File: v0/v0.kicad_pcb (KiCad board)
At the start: 2 copper layers, 101.5 x 83 mm, 2 parts, among them CON1 SNES-CONN

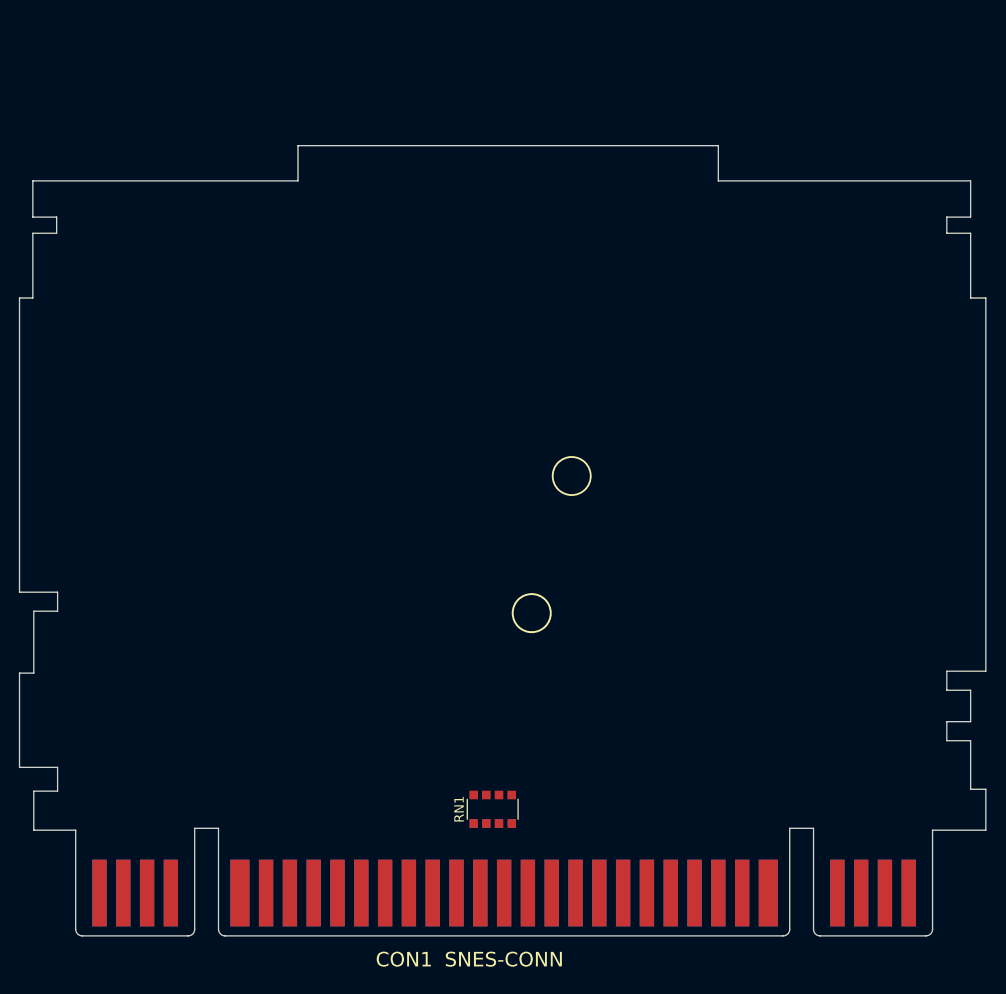
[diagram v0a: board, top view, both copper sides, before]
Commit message: Routed shift registers
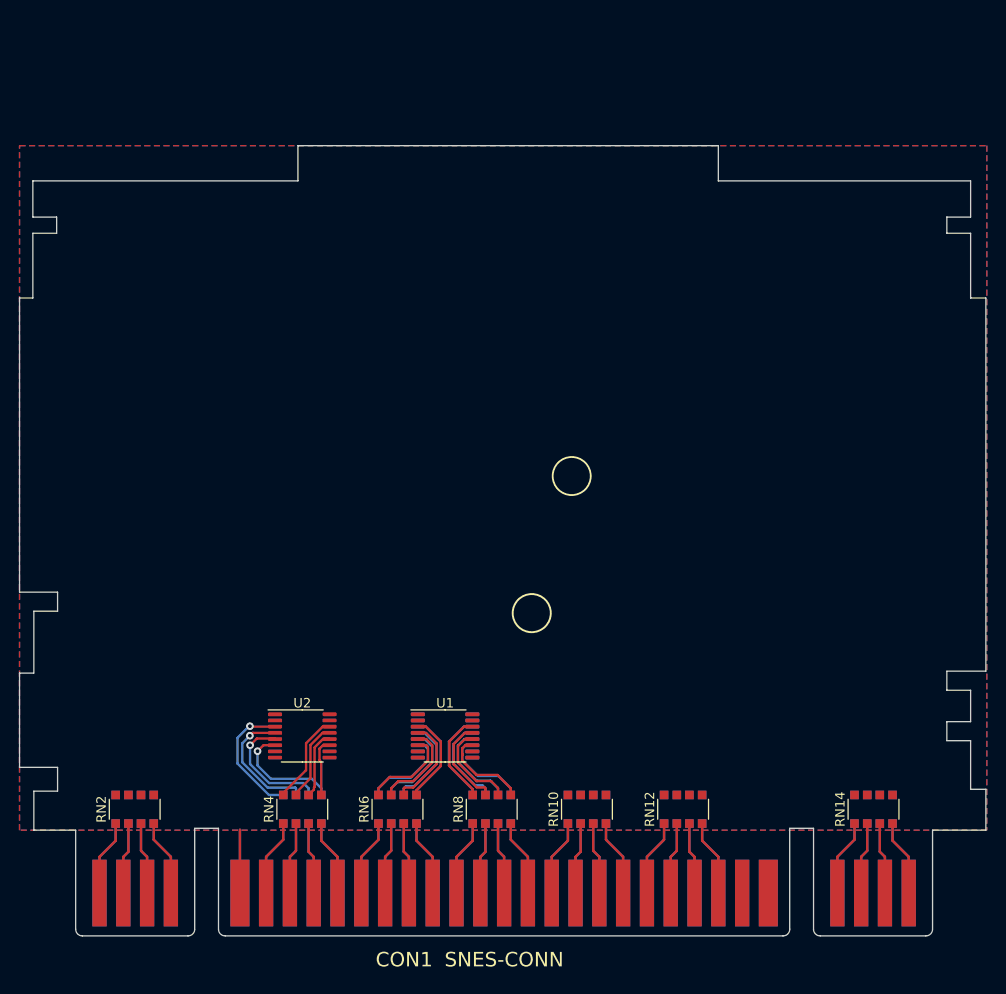
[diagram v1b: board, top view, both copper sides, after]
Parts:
- added RN10: R_Pack04, Resistor_SMD:R_Array_Convex_4x1206, F.Cu at (145.9, 120.5)
- added RN11: R_Pack04, Resistor_SMD:R_Array_Convex_4x1206, B.Cu at (156.0, 120.5)
- added RN12: R_Pack04, Resistor_SMD:R_Array_Convex_4x1206, F.Cu at (156.0, 120.5)
- added RN13: R_Pack04, Resistor_SMD:R_Array_Convex_4x1206, B.Cu at (176.0, 120.5)
- added RN14: R_Pack04, Resistor_SMD:R_Array_Convex_4x1206, F.Cu at (176.0, 120.5)
- added RN2: R_Pack04, Resistor_SMD:R_Array_Convex_4x1206, F.Cu at (98.4, 120.5)
- added RN3: R_Pack04, Resistor_SMD:R_Array_Convex_4x1206, B.Cu at (116.0, 120.5)
- added RN4: R_Pack04, Resistor_SMD:R_Array_Convex_4x1206, F.Cu at (116.0, 120.5)
- added RN5: R_Pack04, Resistor_SMD:R_Array_Convex_4x1206, B.Cu at (126.0, 120.5)
- added RN6: R_Pack04, Resistor_SMD:R_Array_Convex_4x1206, F.Cu at (126.0, 120.5)
- added RN7: R_Pack04, Resistor_SMD:R_Array_Convex_4x1206, B.Cu at (135.9, 120.5)
- added RN8: R_Pack04, Resistor_SMD:R_Array_Convex_4x1206, F.Cu at (135.9, 120.5)
- added RN9: R_Pack04, Resistor_SMD:R_Array_Convex_4x1206, B.Cu at (145.9, 120.5)
- added U1: SN74LV165APWR, Package_SO:TSSOP-16_4.4x5mm_P0.65mm, F.Cu at (131.0, 112.8)
- added U2: SN74LV165APWR, Package_SO:TSSOP-16_4.4x5mm_P0.65mm, F.Cu at (116.0, 112.8)
- added U3: SN74LV165APWR, Package_SO:TSSOP-16_4.4x5mm_P0.65mm, B.Cu at (131.0, 112.8)
- RN1: moved to B.Cu
- moved RN1 37.6 mm to (98.4, 120.5)
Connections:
- RN1 pad 1: /XA3 -> /X~{PAWR}
- RN1 pad 2: /XA2 -> /XPA7
- RN1 pad 3: /XA1 -> /XREFRESH
- RN1 pad 4: /XA0 -> /X~{WRAM}
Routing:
- net /YA13: track 0.00 -> 13.4 mm, vias 0 -> 1
- net /YA12: track 0.00 -> 13.3 mm, vias 0 -> 1
- net GND: track 0.00 -> 13.3 mm
- net /YA14: track 0.00 -> 12.8 mm, vias 0 -> 1
- net /YA15: track 0.00 -> 12.0 mm, vias 0 -> 1
- net /YA5: track 0.00 -> 9.80 mm
- net /YA20: track 0.00 -> 9.75 mm
- net /YA6: track 0.00 -> 9.73 mm
- net /YA4: track 0.00 -> 9.73 mm
- net /YA19: track 0.00 -> 9.72 mm
- net /YA3: track 0.00 -> 9.70 mm
- net /YA7: track 0.00 -> 9.69 mm
- net /YA21: track 0.00 -> 9.68 mm
- net /YA18: track 0.00 -> 9.68 mm
- net /YA2: track 0.00 -> 9.65 mm
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- added copper zone on B.Cu, net GND
- added copper zone on F.Cu, net GND

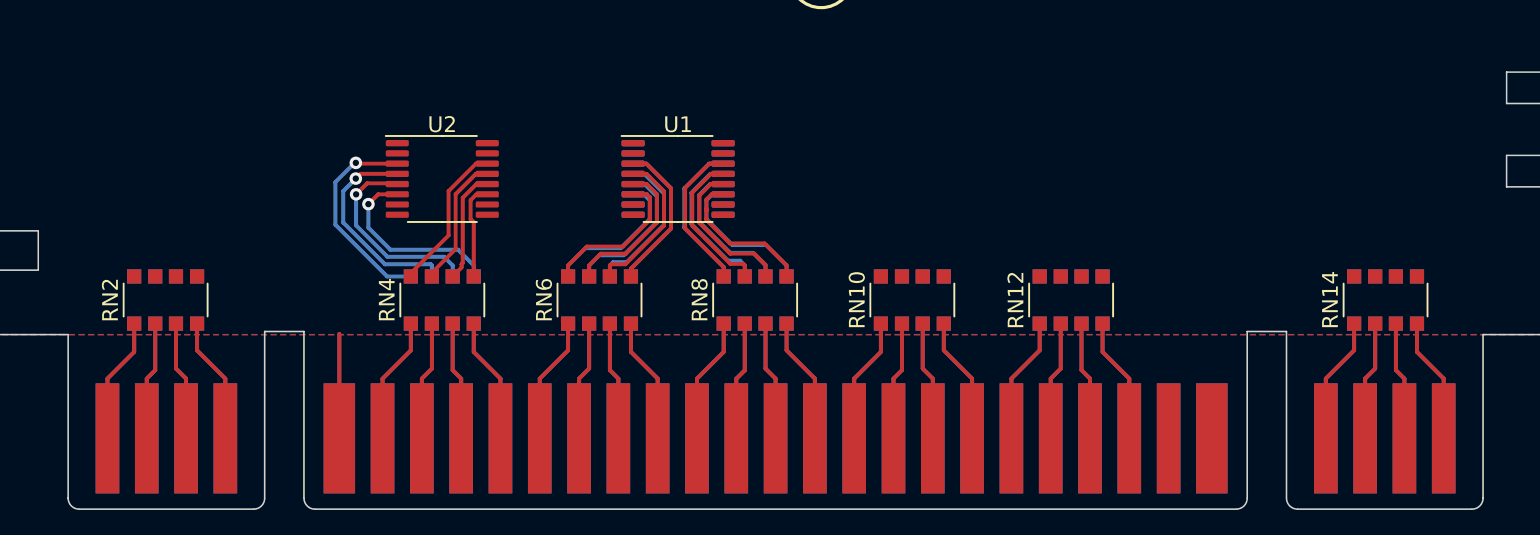
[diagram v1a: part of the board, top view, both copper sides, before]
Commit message: Route through 100R networks and into shift registers for address lines
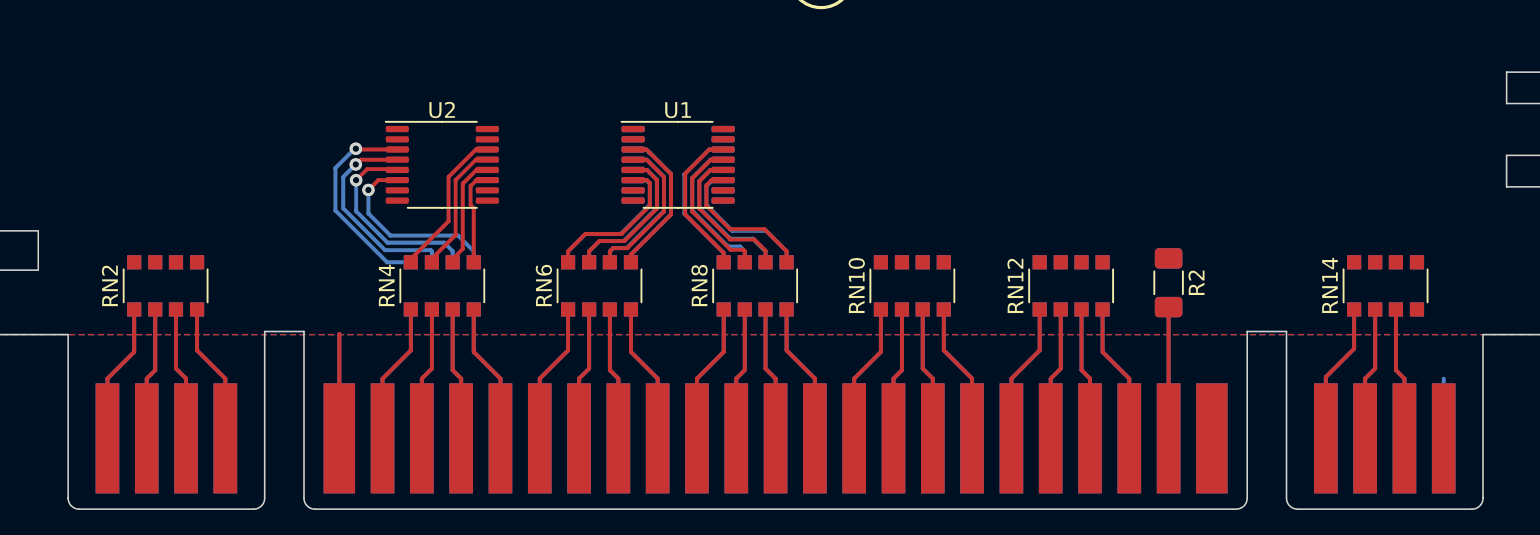
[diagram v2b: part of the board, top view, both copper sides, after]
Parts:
- added R1: 100R, Resistor_SMD:R_1206_3216Metric_Pad1.30x1.75mm_HandSolder, B.Cu at (162.2, 119.4)
- added R2: 100R, Resistor_SMD:R_1206_3216Metric_Pad1.30x1.75mm_HandSolder, F.Cu at (162.2, 119.4)
- RN11, RN9: value R_Pack04 -> 100R
- moved RN1 0.90 mm to (98.4, 119.6)
- moved RN10 0.90 mm to (145.9, 119.6)
- moved RN11 0.90 mm to (156.0, 119.6)
- moved RN12 0.90 mm to (156.0, 119.6)
- moved RN13 0.90 mm to (176.0, 119.6)
- moved RN14 0.90 mm to (176.0, 119.6)
- moved RN2 0.90 mm to (98.4, 119.6)
- moved RN3 0.90 mm to (116.0, 119.6)
- moved RN4 0.90 mm to (116.0, 119.6)
- moved RN5 0.90 mm to (126.0, 119.6)
- moved RN6 0.90 mm to (126.0, 119.6)
- moved RN7 0.90 mm to (135.9, 119.6)
- moved RN8 0.90 mm to (135.9, 119.6)
- moved RN9 0.90 mm to (145.9, 119.6)
- moved U1 0.90 mm to (131.0, 111.9)
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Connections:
- RN1 pad 5: unconnected-(RN1-Pad5) -> /Y~{WRAM}
- RN1 pad 6: unconnected-(RN1-Pad6) -> /YREFRESH
- RN1 pad 7: unconnected-(RN1-Pad7) -> /YPA7
- RN1 pad 8: unconnected-(RN1-Pad8) -> /Y~{PAWR}
- RN13 pad 1: /AUDIO_R -> unconnected-(RN13-Pad1)
- RN14 pad 4: /AUDIO_L -> unconnected-(RN14-Pad4)
- RN14 pad 6: unconnected-(RN14-Pad6) -> /YPA4
- RN14 pad 7: unconnected-(RN14-Pad7) -> /YPA2
- RN14 pad 8: unconnected-(RN14-Pad8) -> /YPA0
- RN2 pad 5: unconnected-(RN2-Pad5) -> /Y~{PARD}
- RN2 pad 6: unconnected-(RN2-Pad6) -> /YPA6
- RN2 pad 7: unconnected-(RN2-Pad7) -> /YEXPAND
- RN2 pad 8: unconnected-(RN2-Pad8) -> /YCLK_21.477MHZ
- U1 pad 1: unconnected-(U1-Pad1) -> /U1~{LD}
- U1 pad 15: unconnected-(U1-Pad15) -> GND
- U1 pad 2: unconnected-(U1-Pad2) -> /CLK_133MHZ
- U1 pad 9: unconnected-(U1-Pad9) -> /U1QH
- U2 pad 1: unconnected-(U2-Pad1) -> /U2~{LD}
- U2 pad 15: unconnected-(U2-Pad15) -> GND
- U2 pad 2: unconnected-(U2-Pad2) -> /CLK_133MHZ
- U2 pad 9: unconnected-(U2-Pad9) -> /U2QH
- U3 pad 1: unconnected-(U3-Pad1) -> /U3~{LD}
- U3 pad 15: unconnected-(U3-Pad15) -> GND
- U3 pad 2: unconnected-(U3-Pad2) -> /CLK_133MHZ
- U3 pad 9: unconnected-(U3-Pad9) -> /U3QH
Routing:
- net /X~{RESET}: track 0.00 -> 8.35 mm
- net /XCPU_CLK: track 0.00 -> 8.35 mm
- net /AUDIO_L: track 8.00 -> 0.00 mm
- net /AUDIO_R: track 8.00 -> 3.80 mm
- net /XPA1: track 8.05 -> 8.95 mm
- net /XPA6: track 7.57 -> 8.47 mm
- net /XD5: track 7.57 -> 8.47 mm
- net /XD1: track 7.57 -> 8.47 mm
- net /XA5: track 7.52 -> 8.42 mm
- net /XA22: track 7.57 -> 8.47 mm
- net /XA18: track 7.52 -> 8.42 mm
- net /XA13: track 7.57 -> 8.47 mm
- net /XA10: track 7.57 -> 8.47 mm
- net /X~{WRAM}: track 8.00 -> 8.90 mm
- net /X~{PAWR}: track 8.05 -> 8.95 mm
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
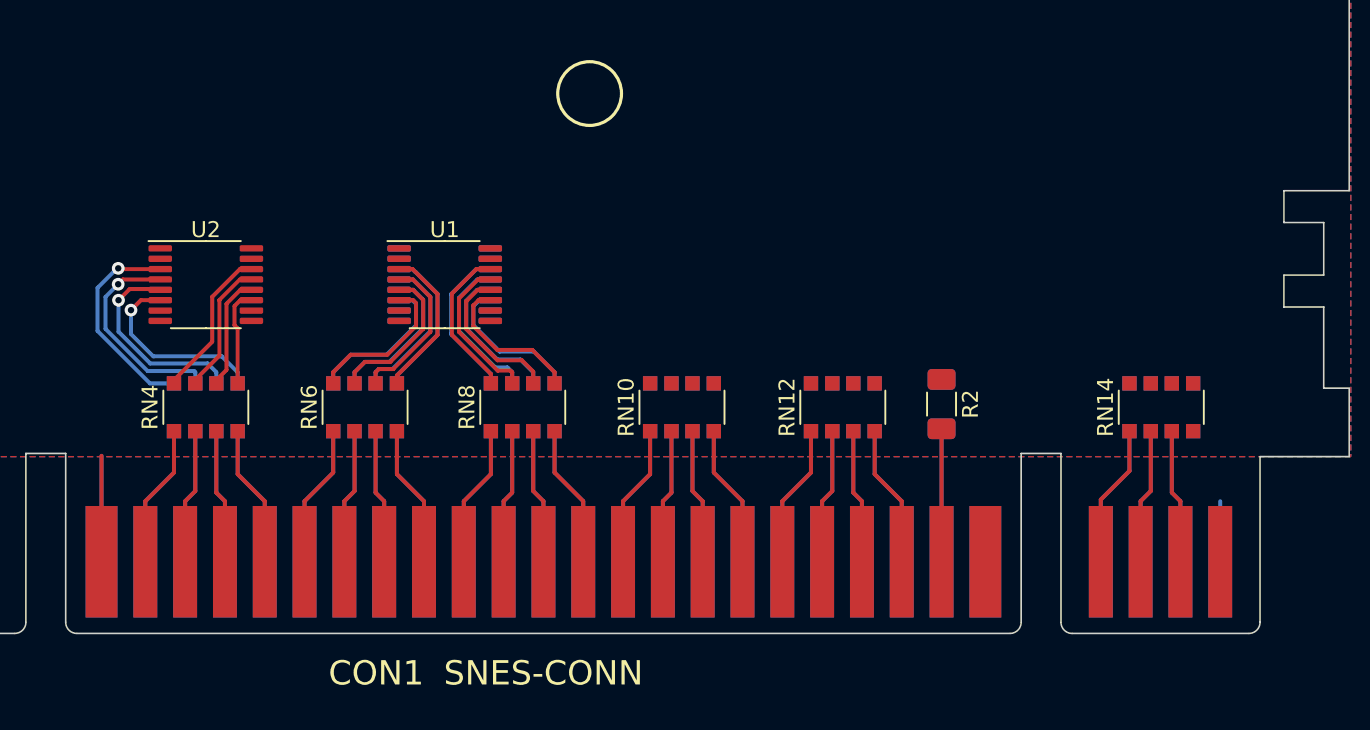
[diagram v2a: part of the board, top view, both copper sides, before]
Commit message: Added PIC12F and 3.3V supply; routed all nets
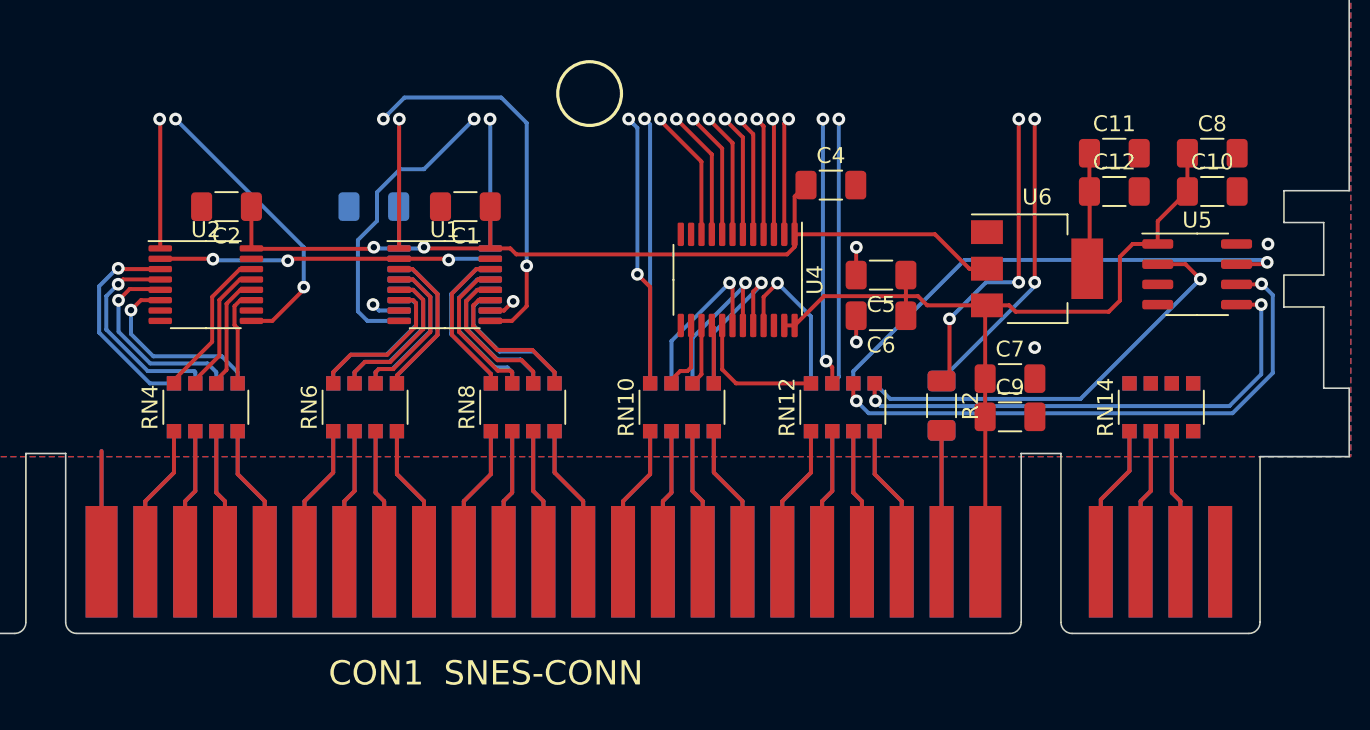
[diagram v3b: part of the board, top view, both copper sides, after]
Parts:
- added C1: 0.1uF, Capacitor_SMD:C_1206_3216Metric_Pad1.33x1.80mm_HandSolder, F.Cu at (132.3, 107.0)
- added C10: 0.1uF, Capacitor_SMD:C_1206_3216Metric_Pad1.33x1.80mm_HandSolder, F.Cu at (179.2, 106.0)
- added C11: 10uF, Capacitor_SMD:C_1206_3216Metric_Pad1.33x1.80mm_HandSolder, F.Cu at (173.1, 103.7)
- added C12: 0.1uF, Capacitor_SMD:C_1206_3216Metric_Pad1.33x1.80mm_HandSolder, F.Cu at (173.1, 106.0)
- added C2: 0.1uF, Capacitor_SMD:C_1206_3216Metric_Pad1.33x1.80mm_HandSolder, F.Cu at (117.3, 107.0)
- added C3: 0.1uF, Capacitor_SMD:C_1206_3216Metric_Pad1.33x1.80mm_HandSolder, B.Cu at (126.5, 107.0)
- added C4: 0.1uF, Capacitor_SMD:C_1206_3216Metric_Pad1.33x1.80mm_HandSolder, F.Cu at (155.2, 105.7)
- added C5: 0.1uF, Capacitor_SMD:C_1206_3216Metric_Pad1.33x1.80mm_HandSolder, F.Cu at (158.4, 111.3)
- added C6: 1uF, Capacitor_SMD:C_1206_3216Metric_Pad1.33x1.80mm_HandSolder, F.Cu at (158.4, 113.8)
- added C7: 0.1uF, Capacitor_SMD:C_1206_3216Metric_Pad1.33x1.80mm_HandSolder, F.Cu at (166.5, 117.8)
- added C8: 1uF, Capacitor_SMD:C_1206_3216Metric_Pad1.33x1.80mm_HandSolder, F.Cu at (179.2, 103.7)
- added C9: 10uF, Capacitor_SMD:C_1206_3216Metric_Pad1.33x1.80mm_HandSolder, F.Cu at (166.5, 120.2)
- added U4: SN74LVC8T245PWR, Package_SO:TSSOP-24_4.4x7.8mm_P0.65mm, F.Cu at (149.4, 111.6)
- added U5: PIC12F629-ISN, Package_SO:SOIC-8_3.9x4.9mm_P1.27mm, F.Cu at (178.2, 111.2)
- added U6: AMS1117-3.3, Package_TO_SOT_SMD:SOT-223-3_TabPin2, F.Cu at (168.2, 110.9)
- moved R1 0.10 mm to (162.2, 119.5)
- moved R2 0.10 mm to (162.2, 119.5)
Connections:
- RN11 pad 7: /YCIC_IN -> /CIC_IN
- RN11 pad 8: /YCIC_CLK -> /CIC_CLK
- RN12 pad 5: /YCIC_RST -> /CIC_RST
- RN12 pad 6: /YCIC_OUT -> /CIC_OUT
- U1 pad 16: unconnected-(U1-Pad16) -> +3.3V
- U2 pad 16: unconnected-(U2-Pad16) -> +3.3V
- U3 pad 16: unconnected-(U3-Pad16) -> +3.3V
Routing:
- net +3.3V: track 0.00 -> 66.9 mm, vias 0 -> 2
- net +5V: track 0.00 -> 53.2 mm
- net /CIC_OUT: track 0.00 -> 36.2 mm, vias 0 -> 2
- net /CIC_RST: track 0.00 -> 32.2 mm, vias 0 -> 2
- net /CIC_IN: track 0.00 -> 31.7 mm, vias 0 -> 1
- net /CIC_CLK: track 0.00 -> 27.0 mm, vias 0 -> 1
- net /U1QH: track 0.00 -> 24.4 mm, vias 0 -> 2
- net /CLK_133MHZ: track 0.00 -> 20.9 mm, vias 0 -> 3
- net /Y~{RESET}: track 0.00 -> 19.7 mm, vias 0 -> 3
- net /YCPU_CLK: track 0.00 -> 18.9 mm, vias 0 -> 2
- net /U3QH: track 0.00 -> 18.8 mm, vias 0 -> 1
- net /U2QH: track 0.00 -> 18.1 mm, vias 0 -> 2
- net /Y~{IRQ}: track 0.00 -> 17.2 mm, vias 0 -> 2
- net /Y~{RD}: track 0.00 -> 16.8 mm, vias 0 -> 2
- net /Y~{WR}: track 0.00 -> 16.8 mm, vias 0 -> 1
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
